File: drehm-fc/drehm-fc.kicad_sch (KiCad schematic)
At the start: 11 parts, among them J1 PWM_OUT, J2 GND, J3 +5V, J4 Conn_01x04, U1 DEV-15583

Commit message: Schematic V1, PCB WIP
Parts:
- removed J1: PWM_OUT, symbol Connector:Conn_01x13_Pin
- removed J2: GND, symbol Connector:Conn_01x13_Pin
- removed J3: +5V, symbol Connector:Conn_01x13_Pin
- added FID1, FID2, FID3: Fiducial, Fiducial:Fiducial_1mm_Mask2mm, symbol Mechanical:Fiducial
- added H1, H2, H3, H4: Mounting Hole, MountingHole:MountingHole_3.2mm_M3_DIN965_Pad, symbol Mechanical:MountingHole_Pad
- added J1: TSW-113-08-T-T-RA, SAMTEC_TSW-113-08-T-T-RA:SAMTEC_TSW-113-08-T-T-RA, symbol TSW_113_08_T_T_RA:TSW-113-08-T-T-RA
- added TP1, TP2: TestPoint, TestPoint:TestPoint_Pad_4.0x4.0mm, symbol Connector:TestPoint
- C1: footprint (none) -> Capacitor_SMD:C_0201_0603Metric
- C2: footprint (none) -> Capacitor_SMD:C_0201_0603Metric; MANUFACTURER (none) -> Murata; Manufacturer P/N (none) -> GRM033Z71A104KE14D
- C3: footprint (none) -> Capacitor_SMD:C_0201_0603Metric; MANUFACTURER (none) -> Murata; Manufacturer P/N (none) -> GRM033R60J225ME47D
- J4: footprint (none) -> Connector_PinHeader_2.54mm:PinHeader_1x04_P2.54mm_Horizontal
- MT1: footprint ICM-42670-P:XDCR_ICM-42670-P -> ICM_42670_P:XDCR_ICM-42670-P
- R1, R2: footprint (none) -> Resistor_SMD:R_0201_0603Metric; MANUFACTURER (none) -> Panasonic; Manufacturer P/N (none) -> ERJ-1GNF1002C
- U1: footprint (none) -> Teensy 4.0:MODULE_DEV-15583
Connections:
- net +3V3: now also J4.1 (Pin_1)
- net Earth: now also J4.4 (Pin_4), H1.1, H2.1, H3.1, H4.1
- net IMU_SCL: now also TP1.1
- net IMU_SDA: now also TP2.1
- net UART RX/I2C SCL: now also J4.2 (Pin_2)
- net UART TX/I2C SDA: now also J4.3 (Pin_3)
- net +5V: now reaches U1.VIN
- net +5V: now also J1.02, J1.05, J1.08, J1.11, J1.14, J1.17, J1.20, J1.23, J1.26, J1.29, J1.32, J1.35, J1.38
- net at U1.0: now also J1.03
- net at U1.1: now also J1.06
- net at U1.10: now also J1.33
- net at U1.11: now also J1.30 (39)
- net at U1.12: now also J1.30 (39)
- net at U1.2: now also J1.09
- net at U1.3: now also J1.12
- net at U1.4: now also J1.15
- net at U1.5: now also J1.18
- net at U1.6: now also J1.21
- net at U1.7: now also J1.24
- net at U1.8: now also J1.27
- net at U1.9: now also J1.30 (39)
- net at U1.G1 (GND): now also J1.01, J1.04, J1.07, J1.10, J1.13, J1.16, J1.19, J1.22, J1.25, J1.28, J1.31, J1.34, J1.37
- no-connect marks 12 -> 10
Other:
- note added: "Probably could use rpp and a bypass cap"
- note removed: "Probably could use ESD protection/rpp and a bypass cap"
- moved on the sheet: C1, C2, C3, J4, MT1, R1, R2

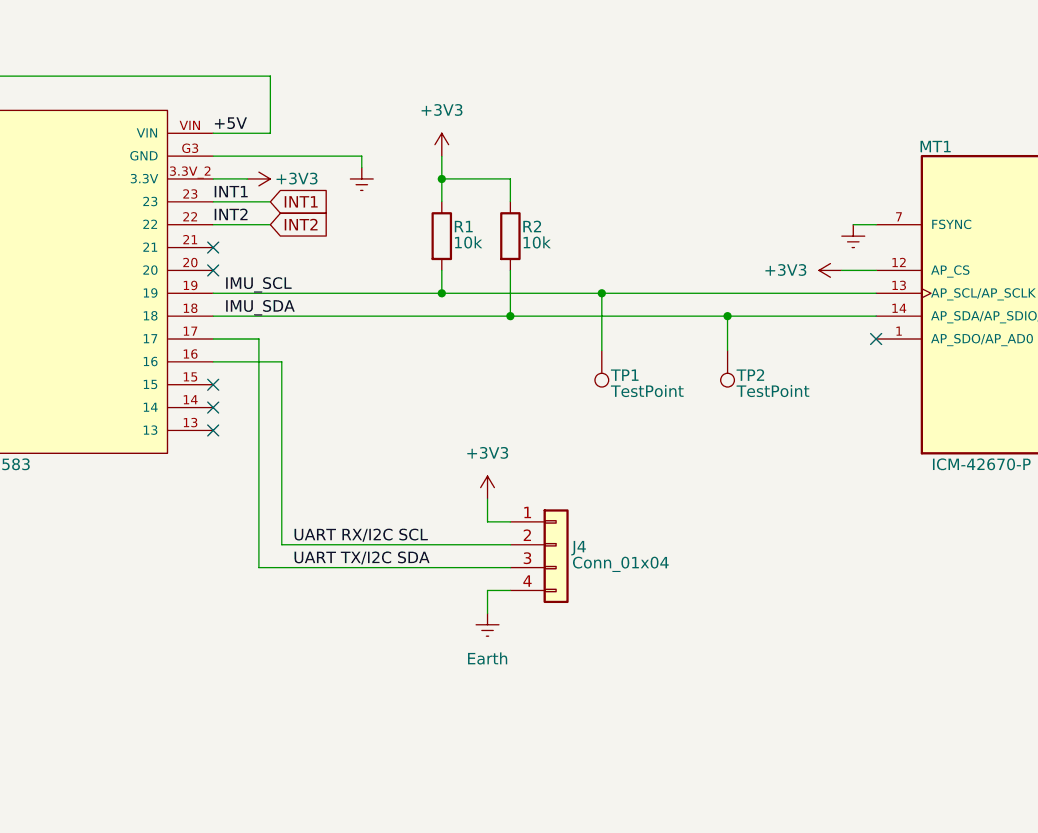
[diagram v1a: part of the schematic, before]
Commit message: design rules set, teensy footprint modified
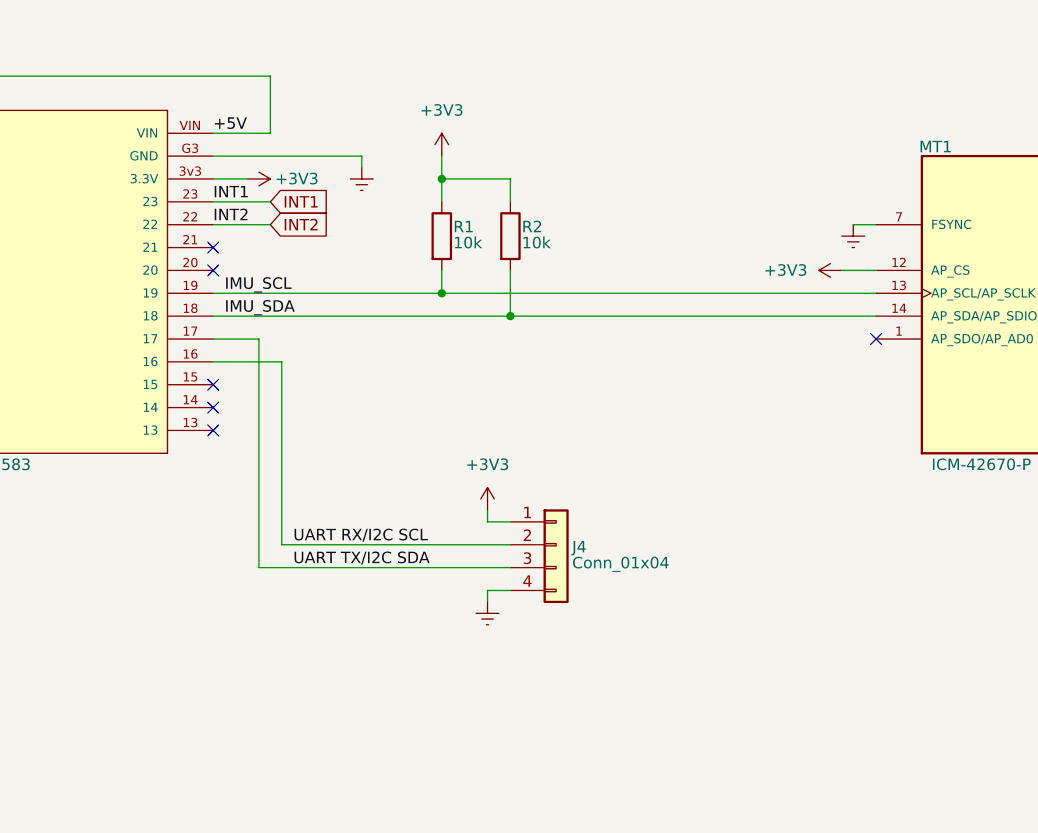
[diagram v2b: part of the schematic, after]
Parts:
- removed TP1, TP2: TestPoint, TestPoint:TestPoint_Pad_4.0x4.0mm, symbol Connector:TestPoint
- J4: footprint Connector_PinHeader_2.54mm:PinHeader_1x04_P2.54mm_Horizontal -> Connector_PinHeader_2.54mm:PinHeader_1x04_P2.54mm_Vertical
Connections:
- net +3V3: now also U1.3v3 (3.3V); no longer U1.3.3V_2 (3.3V)
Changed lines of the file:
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@@
 	)
 	(junction
-		(at 177.8 83.82)
-		(diameter 0)
-		(color 0 0 0 0)
-	)
-	(junction
 		(at 44.45 125.73)
 		(diameter 0)
@@
 	)
 	(junction
-		(at 163.83 81.28)
-		(diameter 0)
-		(color 0 0 0 0)
-	)
-	(junction
 		(at 44.45 93.98)
 		(diameter 0)
@@
 	(wire
 		(pts
-			(xy 177.8 87.63) (xy 177.8 83.82)
-		)
-		(stroke
-			(width 0)
-			(type default)
-		)
-	)
-	(wire
-		(pts
-			(xy 177.8 83.82) (xy 194.31 83.82)
+			(xy 153.67 83.82) (xy 194.31 83.82)
 		)
 		(stroke
@@
 	(wire
 		(pts
-			(xy 146.05 81.28) (xy 163.83 81.28)
+			(xy 146.05 81.28) (xy 194.31 81.28)
 		)
 		(stroke
@@
 	(wire
 		(pts
-			(xy 163.83 81.28) (xy 194.31 81.28)
-		)
-		(stroke
-			(width 0)
-			(type default)
-		)
-	)
-	(wire
-		(pts
 			(xy 245.11 96.52) (xy 248.92 96.52)
 		)
@@
 	(wire
 		(pts
-			(xy 151.13 106.68) (xy 151.13 104.14)
+			(xy 151.13 106.68) (xy 151.13 105.41)
 		)
 		(stroke
@@
 	(wire
 		(pts
-			(xy 153.67 83.82) (xy 177.8 83.82)
-		)
-		(stroke
-			(width 0)
-			(type default)
-		)
-	)
-	(wire
-		(pts
 			(xy 265.43 46.99) (xy 265.43 48.26)
 		)
@@
 	(wire
 		(pts
-			(xy 163.83 87.63) (xy 163.83 81.28)
-		)
-		(stroke
-			(width 0)
-			(type default)
-		)
-	)
-	(wire
-		(pts
 			(xy 44.45 66.04) (xy 44.45 68.58)
 		)
@@
 	(wire
 		(pts
-			(xy 151.13 116.84) (xy 151.13 114.3)
+			(xy 151.13 115.57) (xy 151.13 114.3)
 		)
 		(stroke
@@
 	)
 	(symbol
-		(lib_id "Connector:TestPoint")
-		(at 177.8 87.63 180)
-		(unit 1)
-		(exclude_from_sim no)
-		(in_bom yes)
-		(on_board yes)
-		(dnp no)
-		(property "Reference" "TP2"
-			(at 178.816 90.424 0)
-			(effects
-				(font
-					(size 1.27 1.27)
-				)
-				(justify right)
-			)
-		)
-		(property "Value" "TestPoint"
-			(at 178.816 92.202 0)
-			(effects
-				(font
-					(size 1.27 1.27)
-				)
-				(justify right)
-			)
-		)
-		(property "Footprint" "TestPoint:TestPoint_Pad_4.0x4.0mm"
-			(at 172.72 87.63 0)
-			(effects
-				(font
-					(size 1.27 1.27)
-				)
-				(hide yes)
-			)
-		)
-		(property "Datasheet" "~"
-			(at 172.72 87.63 0)
-			(effects
-				(font
-					(size 1.27 1.27)
-				)
-				(hide yes)
-			)
-		)
-		(property "Description" "test point"
-			(at 177.8 87.63 0)
-			(effects
-				(font
-					(size 1.27 1.27)
-				)
-				(hide yes)
-			)
-		)
-		(property "Manufacturer P/N" ""
-			(at 177.8 87.63 0)
-			(effects
-				(font
-					(size 1.27 1.27)
-				)
-				(hide yes)
-			)
-		)
-		(pin "1"
-		)
-		(instances
-			(project ""
-				(path "/78677983-3e2d-46c3-90bf-4f512dd2e99e"
-					(reference "TP2")
-					(unit 1)
-				)
-			)
-		)
-	)
-	(symbol
 		(lib_id "Device:R")
 		(at 146.05 74.93 0)
@@
 	(symbol
 		(lib_id "power:+3V3")
-		(at 151.13 104.14 0)
+		(at 151.13 105.41 0)
 		(unit 1)
 		(exclude_from_sim no)
@@
 		(fields_autoplaced yes)
 		(property "Reference" "#PWR012"
-			(at 151.13 107.95 0)
+			(at 151.13 109.22 0)
 			(effects
 				(font
@@
 		)
 		(property "Value" "+3V3"
-			(at 151.13 99.06 0)
+			(at 151.13 100.33 0)
 			(effects
 				(font
@@
 		)
 		(property "Footprint" ""
-			(at 151.13 104.14 0)
+			(at 151.13 105.41 0)
 			(effects
 				(font
@@
 		)
 		(property "Datasheet" ""
-			(at 151.13 104.14 0)
+			(at 151.13 105.41 0)
 			(effects
 				(font
@@
 		)
 		(property "Description" "Power symbol creates a global label with name \"+3V3\""
-			(at 151.13 104.14 0)
+			(at 151.13 105.41 0)
 			(effects
 				(font
@@
 	)
 	(symbol
-		(lib_id "Connector:TestPoint")
-		(at 163.83 87.63 180)
-		(unit 1)
-		(exclude_from_sim no)
-		(in_bom yes)
-		(on_board yes)
-		(dnp no)
-		(property "Reference" "TP1"
-			(at 164.846 90.424 0)
-			(effects
-				(font
-					(size 1.27 1.27)
-				)
-				(justify right)
-			)
-		)
-		(property "Value" "TestPoint"
-			(at 164.846 92.202 0)
-			(effects
-				(font
-					(size 1.27 1.27)
-				)
-				(justify right)
-			)
-		)
-		(property "Footprint" "TestPoint:TestPoint_Pad_4.0x4.0mm"
-			(at 158.75 87.63 0)
-			(effects
-				(font
-					(size 1.27 1.27)
-				)
-				(hide yes)
-			)
-		)
-		(property "Datasheet" "~"
-			(at 158.75 87.63 0)
-			(effects
-				(font
-					(size 1.27 1.27)
-				)
-				(hide yes)
-			)
-		)
-		(property "Description" "test point"
-			(at 163.83 87.63 0)
-			(effects
-				(font
-					(size 1.27 1.27)
-				)
-				(hide yes)
-			)
-		)
-		(property "Manufacturer P/N" ""
-			(at 163.83 87.63 0)
-			(effects
-				(font
-					(size 1.27 1.27)
-				)
-				(hide yes)
-			)
-		)
-		(pin "1"
-		)
-		(instances
-			(project ""
-				(path "/78677983-3e2d-46c3-90bf-4f512dd2e99e"
-					(reference "TP1")
-					(unit 1)
-				)
-			)
-		)
-	)
-	(symbol
 		(lib_id "Device:C")
 		(at 260.35 46.99 90)
@@
 	(symbol
 		(lib_id "power:Earth")
-		(at 151.13 116.84 0)
+		(at 151.13 115.57 0)
 		(unit 1)
 		(exclude_from_sim no)
@@
 		(fields_autoplaced yes)
 		(property "Reference" "#PWR013"
-			(at 151.13 123.19 0)
+			(at 151.13 121.92 0)
 			(effects
 				(font
@@
 		)
 		(property "Value" "Earth"
-			(at 151.13 121.92 0)
+			(at 151.13 120.65 0)
 			(effects
 				(font
 					(size 1.27 1.27)
 				)
+				(hide yes)
 			)
 		)
 		(property "Footprint" ""
-			(at 151.13 116.84 0)
+			(at 151.13 115.57 0)
 			(effects
 				(font
@@
 		)
 		(property "Datasheet" "~"
-			(at 151.13 116.84 0)
+			(at 151.13 115.57 0)
 			(effects
 				(font
@@
 		)
 		(property "Description" "Power symbol creates a global label with name \"Earth\""
-			(at 151.13 116.84 0)
+			(at 151.13 115.57 0)
 			(effects
 				(font
@@
 		(pin "7"
 		)
-		(pin "3.3V_2"
+		(pin "3v3"
 		)
 		(pin "12"
@@
 			)
 		)
-		(property "Footprint" "Connector_PinHeader_2.54mm:PinHeader_1x04_P2.54mm_Horizontal"
+		(property "Footprint" "Connector_PinHeader_2.54mm:PinHeader_1x04_P2.54mm_Vertical"
 			(at 158.75 109.22 0)
 			(effects

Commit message: IMU Routing finished, board outline done
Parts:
- J1: footprint SAMTEC_TSW-113-08-T-T-RA:SAMTEC_TSW-113-08-T-T-RA -> TSW-113-08-T-T-RA:SAMTEC_TSW-113-08-T-T-RA
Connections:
- net at J1.30: now also U1.9; no longer U1.11
- net at U1.12: now also J1.39; no longer J1.30 (39)
- new net: J1.36, U1.11
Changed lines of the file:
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@@
 	(wire
 		(pts
+			(xy 69.85 96.52) (xy 85.09 96.52)
+		)
+		(stroke
+			(width 0)
+			(type default)
+		)
+	)
+	(wire
+		(pts
 			(xy 85.09 63.5) (xy 77.47 63.5)
 		)
@@
 	(wire
 		(pts
+			(xy 69.85 91.44) (xy 85.09 91.44)
+		)
+		(stroke
+			(width 0)
+			(type default)
+		)
+	)
+	(wire
+		(pts
 			(xy 137.16 66.04) (xy 120.65 66.04)
 		)
@@
 	(wire
 		(pts
-			(xy 69.85 91.44) (xy 85.09 91.44)
-		)
-		(stroke
-			(width 0)
-			(type default)
-		)
-	)
-	(wire
-		(pts
 			(xy 151.13 106.68) (xy 151.13 105.41)
 		)
@@
 	(wire
 		(pts
-			(xy 69.85 93.98) (xy 85.09 93.98)
+			(xy 69.85 88.9) (xy 85.09 88.9)
 		)
 		(stroke
@@
 	(wire
 		(pts
-			(xy 69.85 88.9) (xy 85.09 88.9)
-		)
-		(stroke
-			(width 0)
-			(type default)
-		)
-	)
-	(wire
-		(pts
 			(xy 137.16 67.31) (xy 137.16 66.04)
 		)
@@
 	(wire
 		(pts
-			(xy 69.85 96.52) (xy 85.09 96.52)
+			(xy 69.85 86.36) (xy 85.09 86.36)
 		)
 		(stroke
@@
 	(wire
 		(pts
-			(xy 69.85 86.36) (xy 85.09 86.36)
+			(xy 77.47 62.23) (xy 44.45 62.23)
 		)
 		(stroke
@@
 	(wire
 		(pts
-			(xy 77.47 62.23) (xy 44.45 62.23)
+			(xy 151.13 115.57) (xy 151.13 114.3)
 		)
 		(stroke
@@
 	(wire
 		(pts
-			(xy 151.13 115.57) (xy 151.13 114.3)
+			(xy 44.45 88.9) (xy 44.45 91.44)
 		)
 		(stroke
@@
 	(wire
 		(pts
-			(xy 44.45 88.9) (xy 44.45 91.44)
+			(xy 151.13 114.3) (xy 153.67 114.3)
 		)
 		(stroke
@@
 	(wire
 		(pts
-			(xy 151.13 114.3) (xy 153.67 114.3)
+			(xy 69.85 93.98) (xy 85.09 93.98)
 		)
 		(stroke
@@
 		)
 		(instances
-			(project ""
+			(project "drehm-fc"
 				(path "/78677983-3e2d-46c3-90bf-4f512dd2e99e"
 					(reference "#PWR010")
@@
 		)
 		(instances
-			(project ""
+			(project "drehm-fc"
 				(path "/78677983-3e2d-46c3-90bf-4f512dd2e99e"
 					(reference "#PWR06")
@@
 		)
 		(instances
-			(project ""
+			(project "drehm-fc"
 				(path "/78677983-3e2d-46c3-90bf-4f512dd2e99e"
 					(reference "C1")
@@
 			)
 		)
-		(property "Footprint" "SAMTEC_TSW-113-08-T-T-RA:SAMTEC_TSW-113-08-T-T-RA"
+		(property "Footprint" "TSW-113-08-T-T-RA:SAMTEC_TSW-113-08-T-T-RA"
 			(at 57.15 60.96 0)
 			(effects
@@
 		(pin "21"
 		)
-		(pin "30"
+		(pin "39"
 		)
 		(pin "19"
@@
 		(pin "-UB"
 		)
-		(pin "30"
+		(pin "36"
 		)
 		(instances
-			(project ""
+			(project "drehm-fc"
 				(path "/78677983-3e2d-46c3-90bf-4f512dd2e99e"
 					(reference "J1")
@@
 		)
 		(instances
-			(project ""
+			(project "drehm-fc"
 				(path "/78677983-3e2d-46c3-90bf-4f512dd2e99e"
 					(reference "R1")
@@
 		)
 		(instances
-			(project ""
+			(project "drehm-fc"
 				(path "/78677983-3e2d-46c3-90bf-4f512dd2e99e"
 					(reference "#PWR02")
@@
 		)
 		(instances
-			(project ""
+			(project "drehm-fc"
 				(path "/78677983-3e2d-46c3-90bf-4f512dd2e99e"
 					(reference "#PWR07")
@@
 		)
 		(instances
-			(project ""
+			(project "drehm-fc"
 				(path "/78677983-3e2d-46c3-90bf-4f512dd2e99e"
 					(reference "#PWR09")
@@
 		)
 		(instances
-			(project ""
+			(project "drehm-fc"
 				(path "/78677983-3e2d-46c3-90bf-4f512dd2e99e"
 					(reference "C2")
@@
 		)
 		(instances
-			(project ""
+			(project "drehm-fc"
 				(path "/78677983-3e2d-46c3-90bf-4f512dd2e99e"
 					(reference "#PWR01")
@@
 		)
 		(instances
-			(project ""
+			(project "drehm-fc"
 				(path "/78677983-3e2d-46c3-90bf-4f512dd2e99e"
 					(reference "#PWR012")
@@
 		)
 		(instances
-			(project ""
+			(project "drehm-fc"
 				(path "/78677983-3e2d-46c3-90bf-4f512dd2e99e"
 					(reference "R2")
@@
 		)
 		(instances
-			(project ""
+			(project "drehm-fc"
 				(path "/78677983-3e2d-46c3-90bf-4f512dd2e99e"
 					(reference "#PWR04")
@@
 		)
 		(instances
-			(project ""
+			(project "drehm-fc"
 				(path "/78677983-3e2d-46c3-90bf-4f512dd2e99e"
 					(reference "#PWR03")
@@
 		)
 		(instances
-			(project ""
+			(project "drehm-fc"
 				(path "/78677983-3e2d-46c3-90bf-4f512dd2e99e"
 					(reference "#PWR05")
@@
 		)
 		(instances
-			(project ""
+			(project "drehm-fc"
 				(path "/78677983-3e2d-46c3-90bf-4f512dd2e99e"
 					(reference "C3")
@@
 		)
 		(instances
-			(project ""
+			(project "drehm-fc"
 				(path "/78677983-3e2d-46c3-90bf-4f512dd2e99e"
 					(reference "H1")
@@
 		)
 		(instances
-			(project ""
+			(project "drehm-fc"
 				(path "/78677983-3e2d-46c3-90bf-4f512dd2e99e"
 					(reference "#PWR013")
@@
 		)
 		(instances
-			(project ""
+			(project "drehm-fc"
 				(path "/78677983-3e2d-46c3-90bf-4f512dd2e99e"
 					(reference "MT1")
@@
 		)
 		(instances
-			(project ""
+			(project "drehm-fc"
 				(path "/78677983-3e2d-46c3-90bf-4f512dd2e99e"
 					(reference "#PWR08")
@@
 		)
 		(instances
-			(project ""
+			(project "drehm-fc"
 				(path "/78677983-3e2d-46c3-90bf-4f512dd2e99e"
 					(reference "U1")
@@
 		)
 		(instances
-			(project ""
+			(project "drehm-fc"
 				(path "/78677983-3e2d-46c3-90bf-4f512dd2e99e"
 					(reference "FID1")
@@
 		)
 		(instances
-			(project ""
+			(project "drehm-fc"
 				(path "/78677983-3e2d-46c3-90bf-4f512dd2e99e"
 					(reference "#PWR011")
@@
 		)
 		(instances
-			(project ""
+			(project "drehm-fc"
 				(path "/78677983-3e2d-46c3-90bf-4f512dd2e99e"
 					(reference "J4")
@@
 		)
 		(instances
-			(project ""
+			(project "drehm-fc"
 				(path "/78677983-3e2d-46c3-90bf-4f512dd2e99e"
 					(reference "#PWR014")

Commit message: Routing mostly done, finishing touches WIP
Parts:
- MT1: footprint ICM_42670_P:XDCR_ICM-42670-P -> ICM-42670-P:XDCR_ICM-42670-P
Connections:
- net Earth: now also J1.01, J1.04, J1.07, J1.10, J1.13, J1.16, J1.19, J1.22, J1.25, J1.28, J1.31, J1.34, J1.37, U1.G1 (GND)

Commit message: Manufacturability changes, silkscreen update
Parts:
- C1: MANUFACTURER (none) -> Murata; MPN (none) -> C161472; Manufacturer P/N (none) -> GRM033R61C103KA12D
- C2: MPN (none) -> C161494
- C3: MPN (none) -> C76933
- J1, J4, U1: now left out of the parts list
- MT1: footprint ICM-42670-P:XDCR_ICM-42670-P -> ICM_42670_P:XDCR_ICM-42670-P; MPN (none) -> C3288646
- R1, R2: MPN (none) -> C490808; Manufacturer P/N ERJ-1GNF1002C -> ERA1AEB103C
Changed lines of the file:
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@@
 			)
 		)
-		(property "Manufacturer P/N" ""
+		(property "Manufacturer P/N" "GRM033R61C103KA12D "
+			(at 260.35 71.12 0)
+			(effects
+				(font
+					(size 1.27 1.27)
+				)
+				(hide yes)
+			)
+		)
+		(property "MANUFACTURER" "Murata"
+			(at 260.35 71.12 0)
+			(effects
+				(font
+					(size 1.27 1.27)
+				)
+				(hide yes)
+			)
+		)
+		(property "MPN" "C161472"
 			(at 260.35 71.12 0)
 			(effects
@@
 		(unit 1)
 		(exclude_from_sim no)
-		(in_bom yes)
+		(in_bom no)
 		(on_board yes)
 		(dnp no)
@@
 			)
 		)
-		(property "Manufacturer P/N" "ERJ-1GNF1002C"
+		(property "Manufacturer P/N" "ERA1AEB103C"
 			(at 146.05 74.93 0)
 			(effects
@@
 		)
 		(property "MANUFACTURER" "Panasonic"
+			(at 146.05 74.93 0)
+			(effects
+				(font
+					(size 1.27 1.27)
+				)
+				(hide yes)
+			)
+		)
+		(property "MPN" "C490808"
 			(at 146.05 74.93 0)
 			(effects
@@
 			)
 		)
+		(property "MPN" "C161494"
+			(at 260.35 57.15 0)
+			(effects
+				(font
+					(size 1.27 1.27)
+				)
+				(hide yes)
+			)
+		)
 		(pin "2"
 		)
@@
 			)
 		)
-		(property "Manufacturer P/N" "ERJ-1GNF1002C"
+		(property "Manufacturer P/N" "ERA1AEB103C"
 			(at 153.67 74.93 0)
 			(effects
@@
 		)
 		(property "MANUFACTURER" "Panasonic"
+			(at 153.67 74.93 0)
+			(effects
+				(font
+					(size 1.27 1.27)
+				)
+				(hide yes)
+			)
+		)
+		(property "MPN" "C490808"
 			(at 153.67 74.93 0)
 			(effects
@@
 			)
 		)
+		(property "MPN" "C76933"
+			(at 260.35 46.99 0)
+			(effects
+				(font
+					(size 1.27 1.27)
+				)
+				(hide yes)
+			)
+		)
 		(pin "2"
 		)
@@
 			)
 		)
-		(property "Footprint" "ICM-42670-P:XDCR_ICM-42670-P"
+		(property "Footprint" "ICM_42670_P:XDCR_ICM-42670-P"
 			(at 219.71 78.74 0)
 			(effects
@@
 			)
 		)
+		(property "MPN" "C3288646"
+			(at 219.71 78.74 0)
+			(effects
+				(font
+					(size 1.27 1.27)
+				)
+				(hide yes)
+			)
+		)
 		(pin "11"
 		)
@@
 		(unit 1)
 		(exclude_from_sim no)
-		(in_bom yes)
+		(in_bom no)
 		(on_board yes)
 		(dnp no)
@@
 		(unit 1)
 		(exclude_from_sim no)
-		(in_bom yes)
-		(on_board yes)
-		(dnp no)
+		(in_bom no)
+		(on_board yes)
+		(dnp no)
